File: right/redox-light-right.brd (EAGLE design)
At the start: 161 x 125.5 mm, 137 parts, among them IC36 STM32F103TXUX, X1 USBMICRO_B, X2 AUDIO-JACKSMD

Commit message: some improoves
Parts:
- added R4: 10k, netcat:R0402
- TP1: value (none) -> CLK
- TP2: value (none) -> IO
- moved C22 1.56 mm to (-34.5, 112.9)
- moved C20 1.00 mm to (-34.4, 107.4)
- moved C21 1.00 mm to (-37.8, 109.9)
- moved QZ1 1.00 mm to (-34.9, 109.6)
- moved R2 1.00 mm to (-34.4, 104.2)
- moved R3 1.00 mm to (-34.4, 105.4)
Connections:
- new net N$35: IC36.4, R4.1
- net VCC: now also R4.2; no longer IC36.4
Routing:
- net N$35: track 0.00 -> 4.73 mm
- net VCC: track 55.2 -> 59.8 mm, vias 6 -> 7
- net COL2: track 96.0 -> 97.8 mm
- net ROW4: track 270.9 -> 272.5 mm
- net COL1: track 121.1 -> 122.7 mm
- net COL0: track 143.2 -> 144.4 mm
- net COL6: track 208.7 -> 209.9 mm
- net COL5: track 162.6 -> 163.7 mm
- net N$23: track 4.43 -> 5.43 mm
- net N$31: track 7.39 -> 8.39 mm
- net COL4: track 139.4 -> 140.3 mm
- net COL3: track 113.6 -> 114.3 mm
- net ROW3: track 277.2 -> 277.9 mm
- net ROW2: track 247.2 -> 247.7 mm
- net GND: vias 4 -> 40

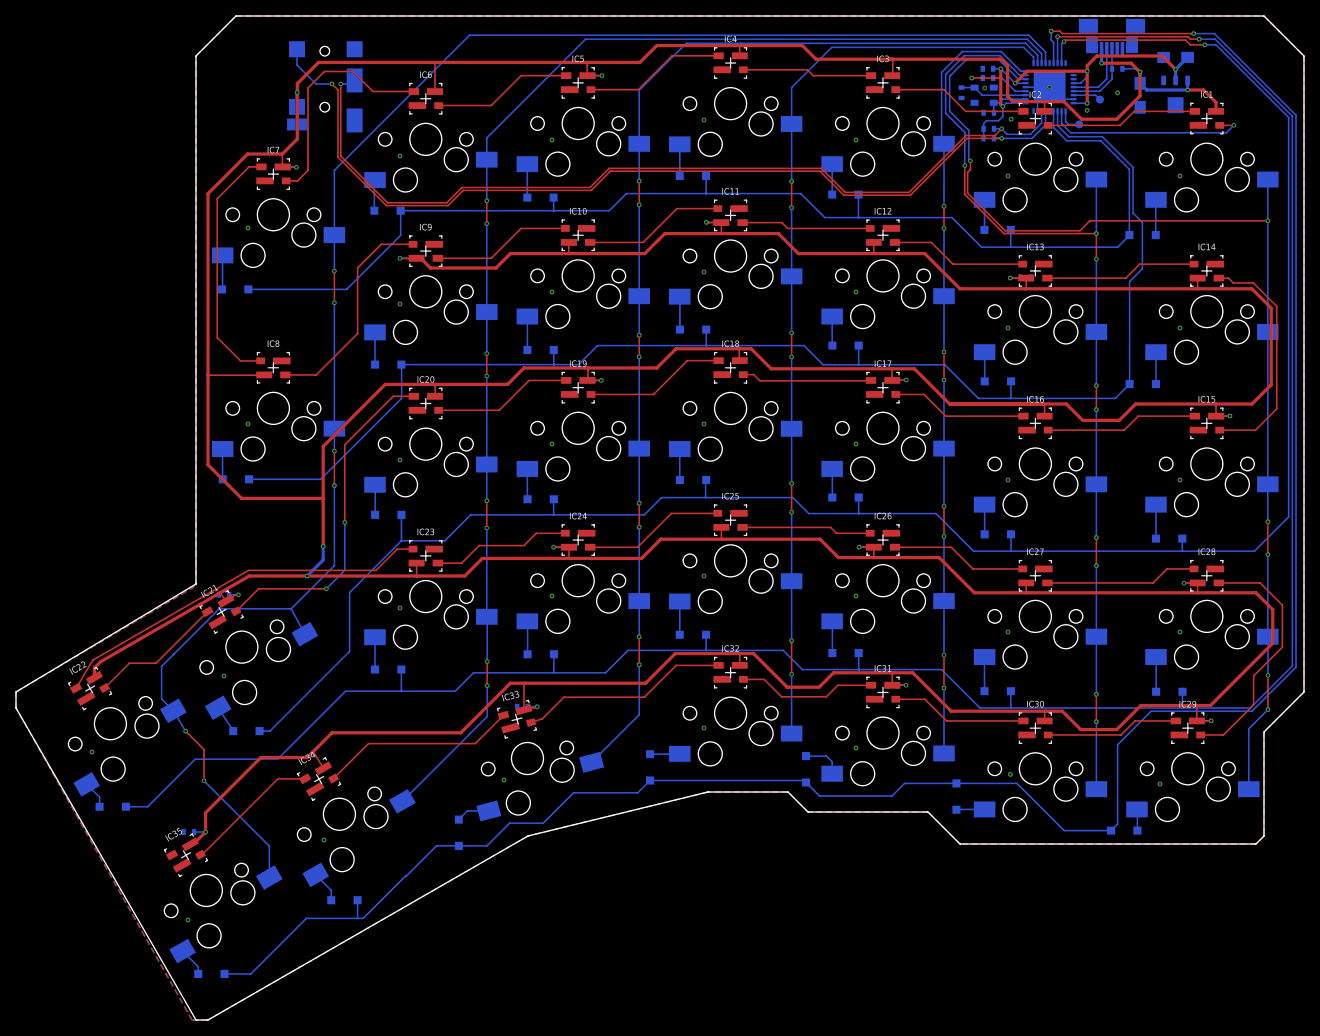
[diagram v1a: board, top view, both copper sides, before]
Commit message: drc warn fixes
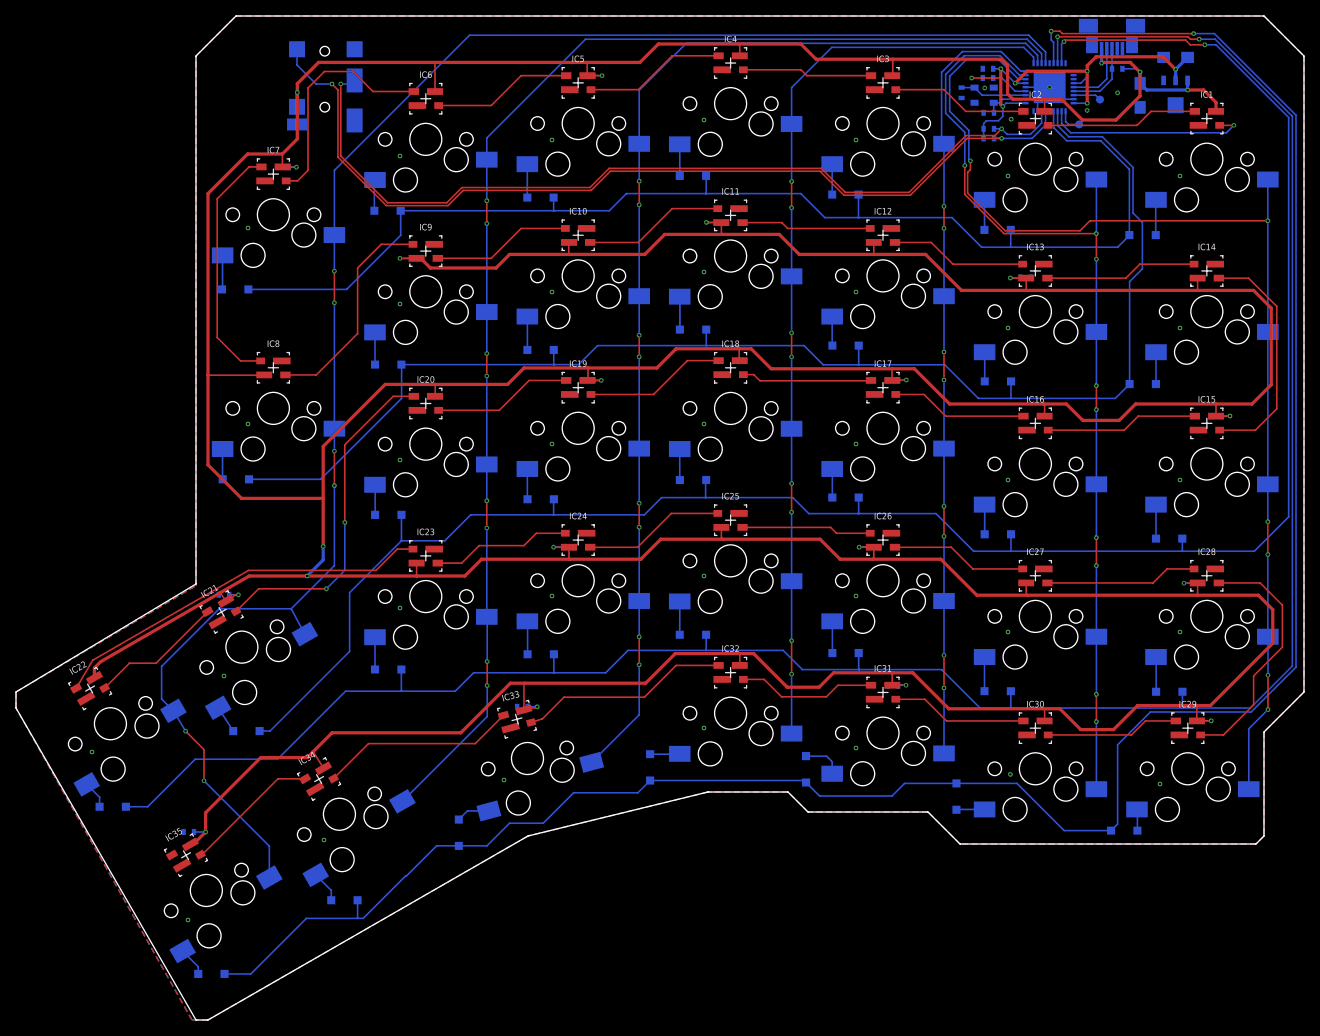
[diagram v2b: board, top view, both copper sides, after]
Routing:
- net 5V: track 916.3 -> 906.6 mm

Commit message: lm1117 pkg fix
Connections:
- net GND: no longer IC37.4
- net VCC: now also IC37.4
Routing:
- net VCC: track 59.7 -> 62.8 mm
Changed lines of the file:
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@@
 <drawing>
 <settings>
-<setting alwaysvectorfont="yes"/>
+<setting alwaysvectorfont="no"/>
 <setting verticaltext="up"/>
 </settings>
@@
 <wire x1="-32.9" y1="108.45" x2="-32.65" y2="108.2" width="0.4064" layer="1"/>
 <wire x1="-32.9" y1="111.8" x2="-32.9" y2="108.45" width="0.4064" layer="1"/>
+<contactref element="IC37" pad="4"/>
+<wire x1="-11.05" y1="111.45" x2="-11.05" y2="108.35" width="0.4064" layer="16"/>
 </signal>
 <signal name="GND">
@@
 <contactref element="X1" pad="6"/>
 <contactref element="X1" pad="GND"/>
-<contactref element="IC37" pad="4"/>
 <contactref element="C1" pad="-"/>
 <contactref element="C3" pad="2"/>
@@
 <wire x1="-124.975" y1="74.63325" x2="-125.00825" y2="74.6" width="0.2032" layer="1"/>
 <wire x1="-125.00825" y1="74.6" x2="-132" y2="74.6" width="0.2032" layer="1"/>
-<wire x1="-9.55" y1="110.25" x2="-14.655" y2="110.25" width="0.4064" layer="16"/>
-<wire x1="-14.655" y1="110.25" x2="-15.485" y2="111.08" width="0.4064" layer="16"/>
 <wire x1="-18.5" y1="106.5" x2="-15.5" y2="109.5" width="0.4064" layer="1"/>
 <wire x1="-15.5" y1="109.5" x2="-15.5" y2="112.485" width="0.4064" layer="1"/>
@@
 <wire x1="-27.6" y1="109.1" x2="-27.4" y2="109.1" width="0.4064" layer="1"/>
 <wire x1="-20.3" y1="113.6" x2="-20.2" y2="113.7" width="0.4064" layer="1"/>
+<wire x1="-9.55" y1="110.25" x2="-10.3" y2="109.5" width="0.4064" layer="1"/>
+<wire x1="-10.3" y1="109.5" x2="-15.5" y2="109.5" width="0.4064" layer="1"/>
 </signal>
 <signal name="N$23">
